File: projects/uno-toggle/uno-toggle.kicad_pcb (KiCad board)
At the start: 2 copper layers, 68.6 x 53.3 mm, 9 parts, among them SW1 BTN1, SW2 BTN2

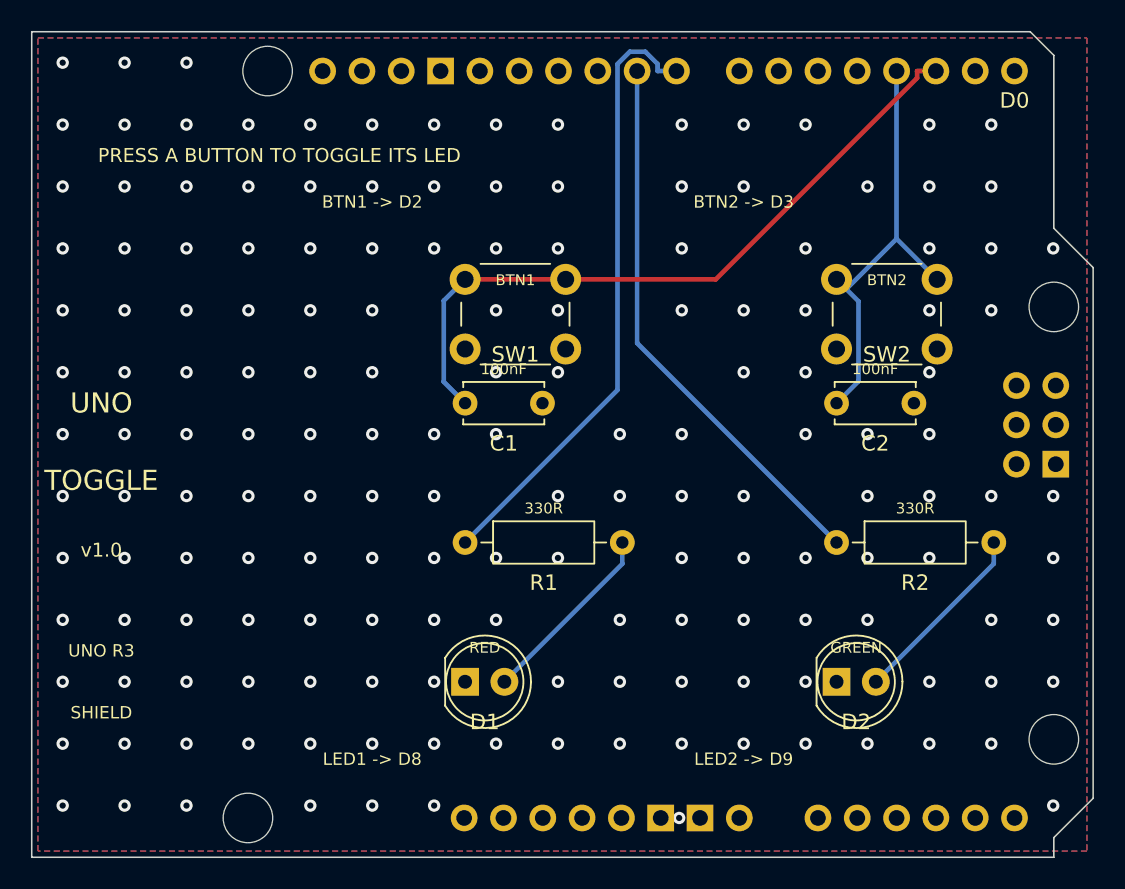
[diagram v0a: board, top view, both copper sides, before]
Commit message: fix(MD-T11): derive via/stitch spacing from fab rules (no flaky hole_to_hole)
Co-Authored-By: Claude Opus 5.5 <noreply@anthropic.com>
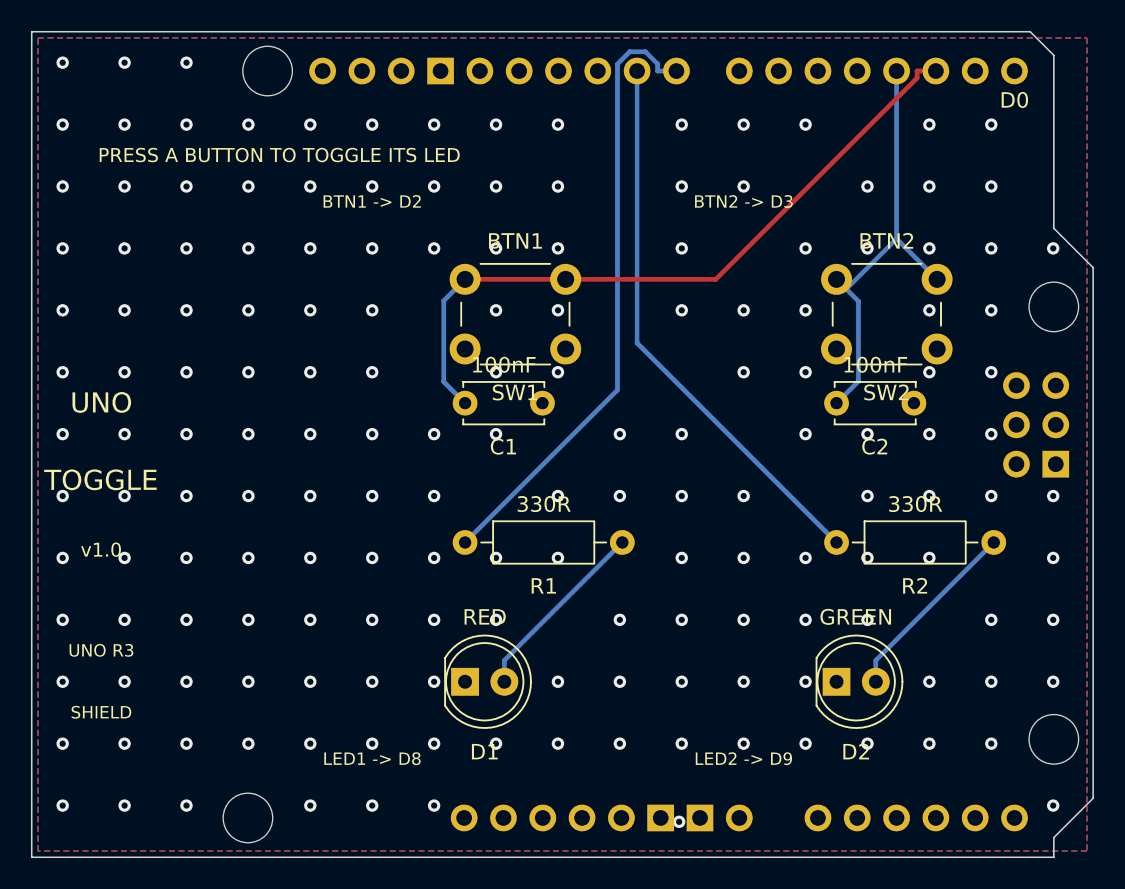
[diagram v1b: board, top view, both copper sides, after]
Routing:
- net GND: vias 166 -> 169

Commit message: feat(P1-T9b): fixtures on the parts registry (pins by function, strict mode)
Co-Authored-By: Claude Opus 5.5 <noreply@anthropic.com>
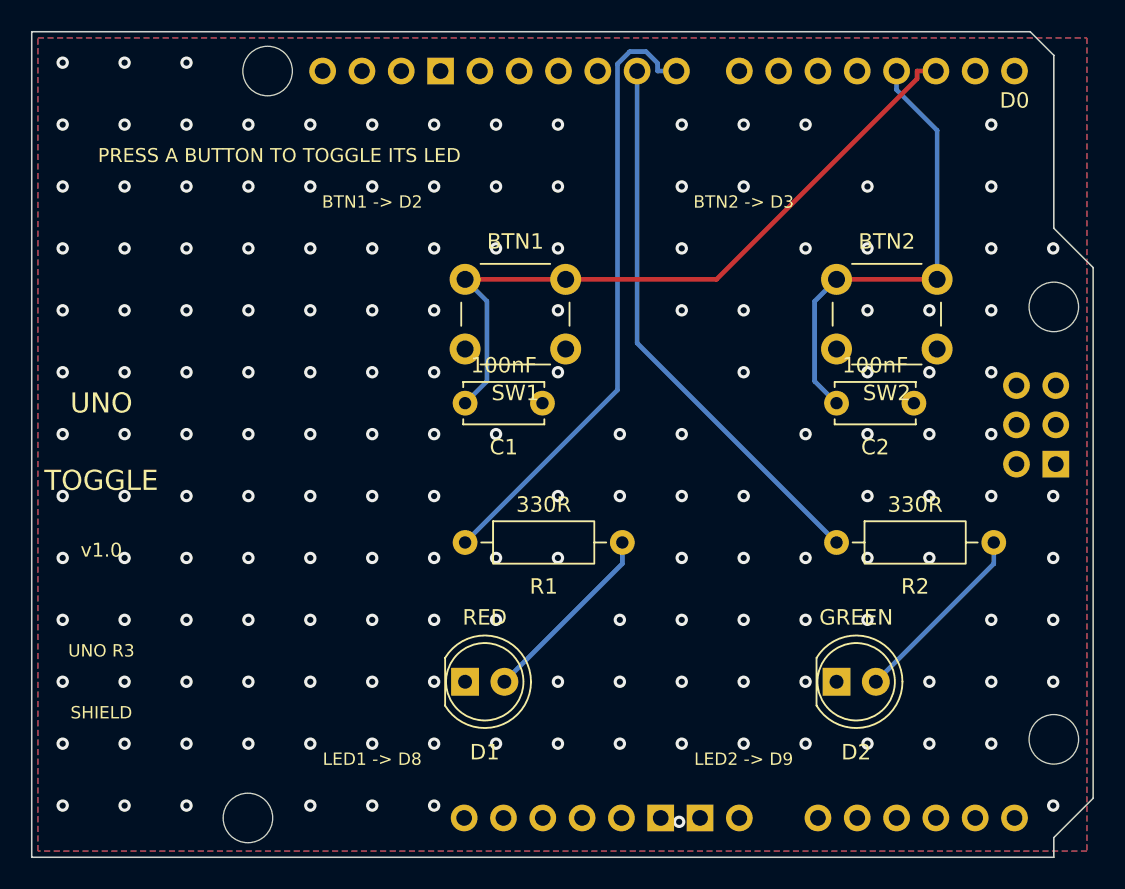
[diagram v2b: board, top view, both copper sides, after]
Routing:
- net /BTN2: track 28.3 -> 30.2 mm
- net GND: vias 169 -> 166

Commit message: fix(P1-T9b): keep LCSC ids, package family match, PR-BYNAME
Co-Authored-By: Claude Opus 5.5 <noreply@anthropic.com>
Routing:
- net /BTN2: track 30.2 -> 28.3 mm
- net GND: vias 166 -> 169
